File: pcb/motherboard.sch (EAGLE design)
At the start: 22 parts, among them U1 MIC5219 3.3V

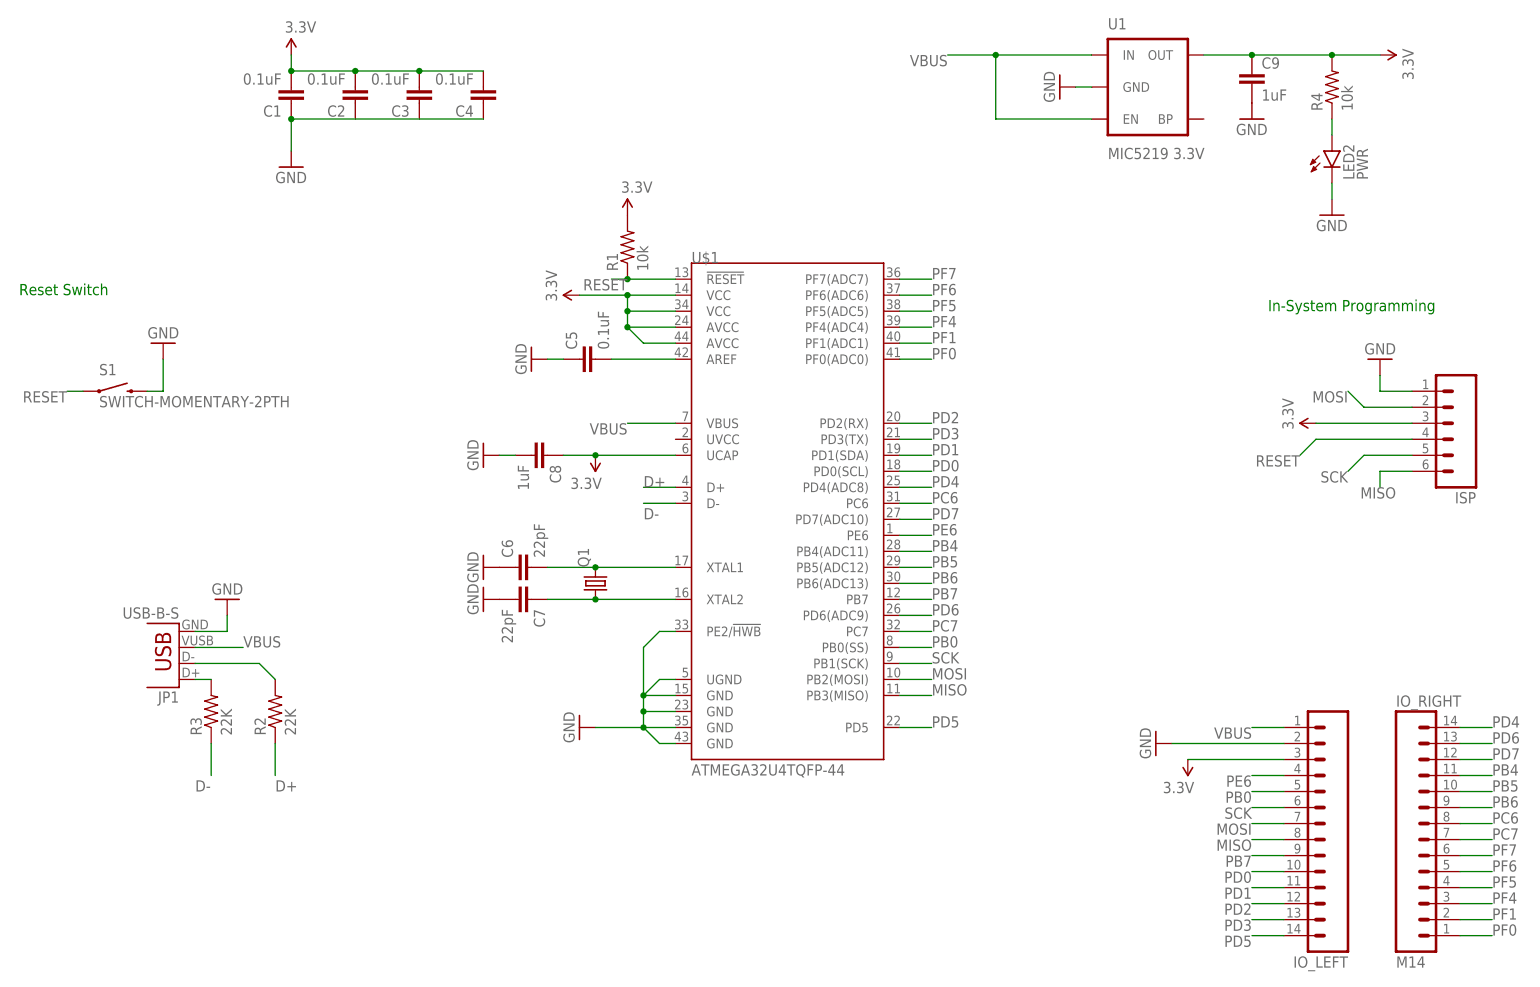
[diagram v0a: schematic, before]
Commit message: - Updated PCB to include bigger components, 805 instead of 804 - Improved PCB layout
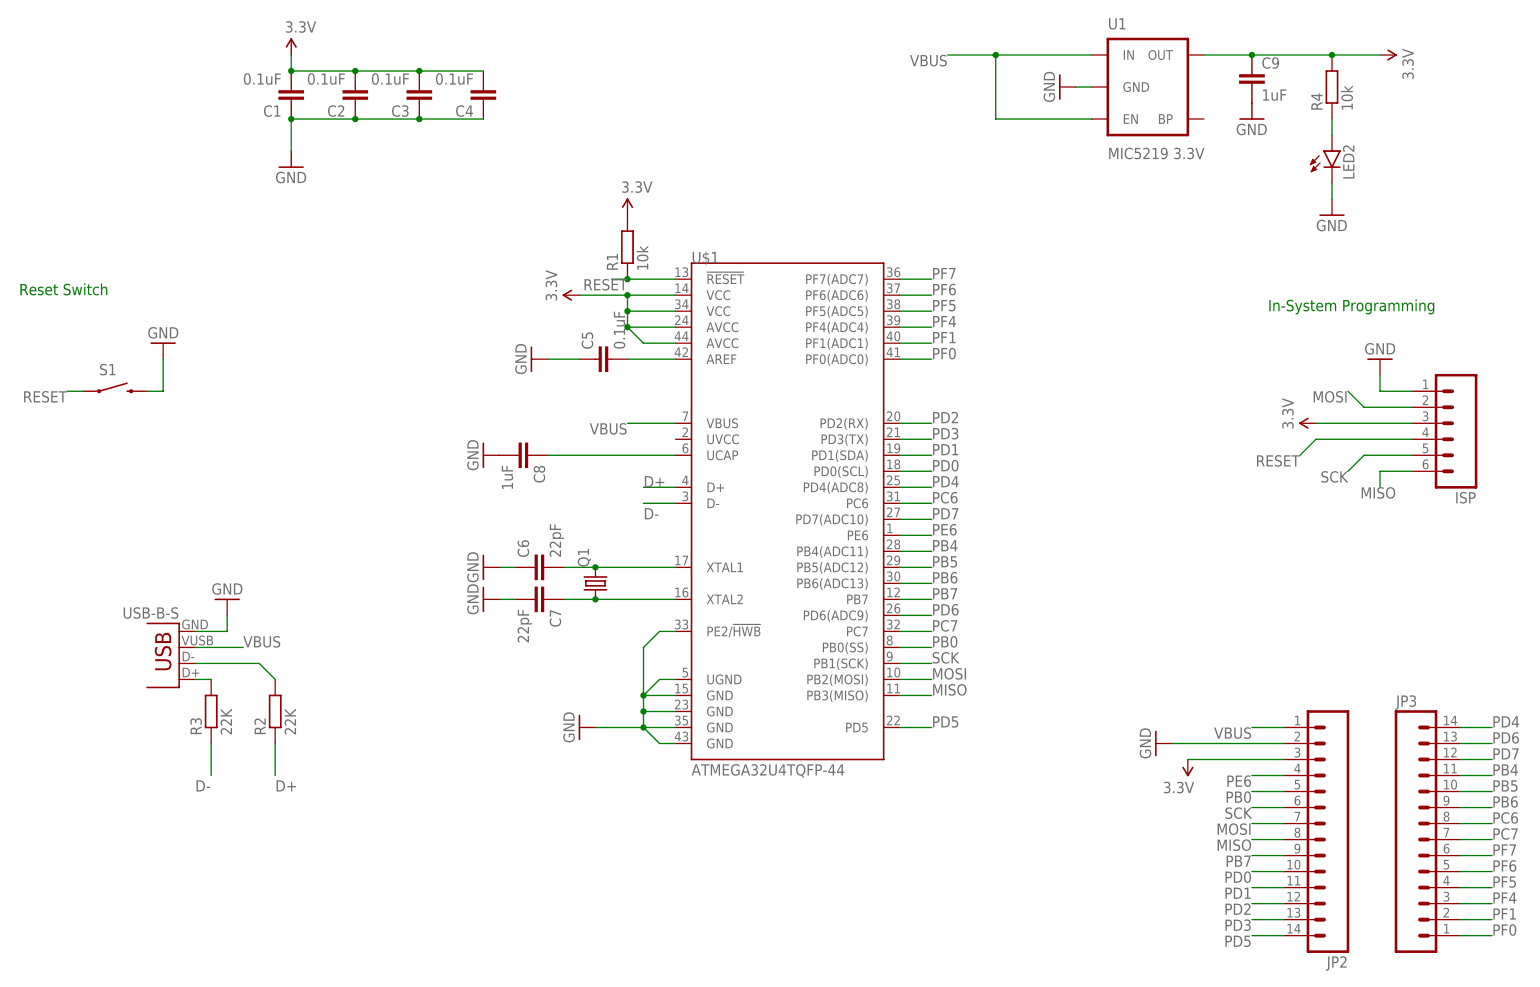
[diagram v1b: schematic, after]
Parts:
- C1, C2, C3, C4, C5: device SparkFun-Capacitors:0.1UF-25V(+80/-20%)(0603) -> ELL-i-Passives:C0805
- C6, C7: device SparkFun-Capacitors:22PF-50V-5%(0603) -> ELL-i-Passives:C0805
- C8, C9: device SparkFun-Capacitors:1UF-25V-10%(0805) -> ELL-i-Passives:C0805
- LED2: value PWR -> (none)
- R1: device SparkFun-Resistors:10KOHM-1/4W-1%(PTH)HORIZ -> ELL-i-Passives:R0805
- R2, R3: device SparkFun-Resistors:22KOHM1/10W1%(0603) -> ELL-i-Passives:R0805
- R4: device SparkFun-Resistors:10KOHM-1/4W-1%(PTH)HORIZ-KIT -> ELL-i-Passives:R0805
- renumbered IO_LEFT to JP2, IO_RIGHT to JP3
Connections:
- new net N$10: C8.1, U$1.UCAP
- net 3.3V: no longer C8.1, U$1.UCAP
- net GND: now also C2.1, C3.1
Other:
- moved on the sheet: C5, C6, C7, C8
